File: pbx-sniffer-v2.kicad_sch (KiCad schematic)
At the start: 0 parts

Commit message: finish initial supporting components for mcu
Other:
- sheet MCU ports: added linectrl0, linectrl1, linectrl10, linectrl11, linectrl12, linectrl13, linectrl14, linectrl15, linectrl2, linectrl3, linectrl4, linectrl5, linectrl6, linectrl7, linectrl8, linectrl9, shiftClk, shiftInh, shiftLd, shiftOut, spi0clk, spi0cs0, spi0miso, spi0mosi, usb5V; removed none

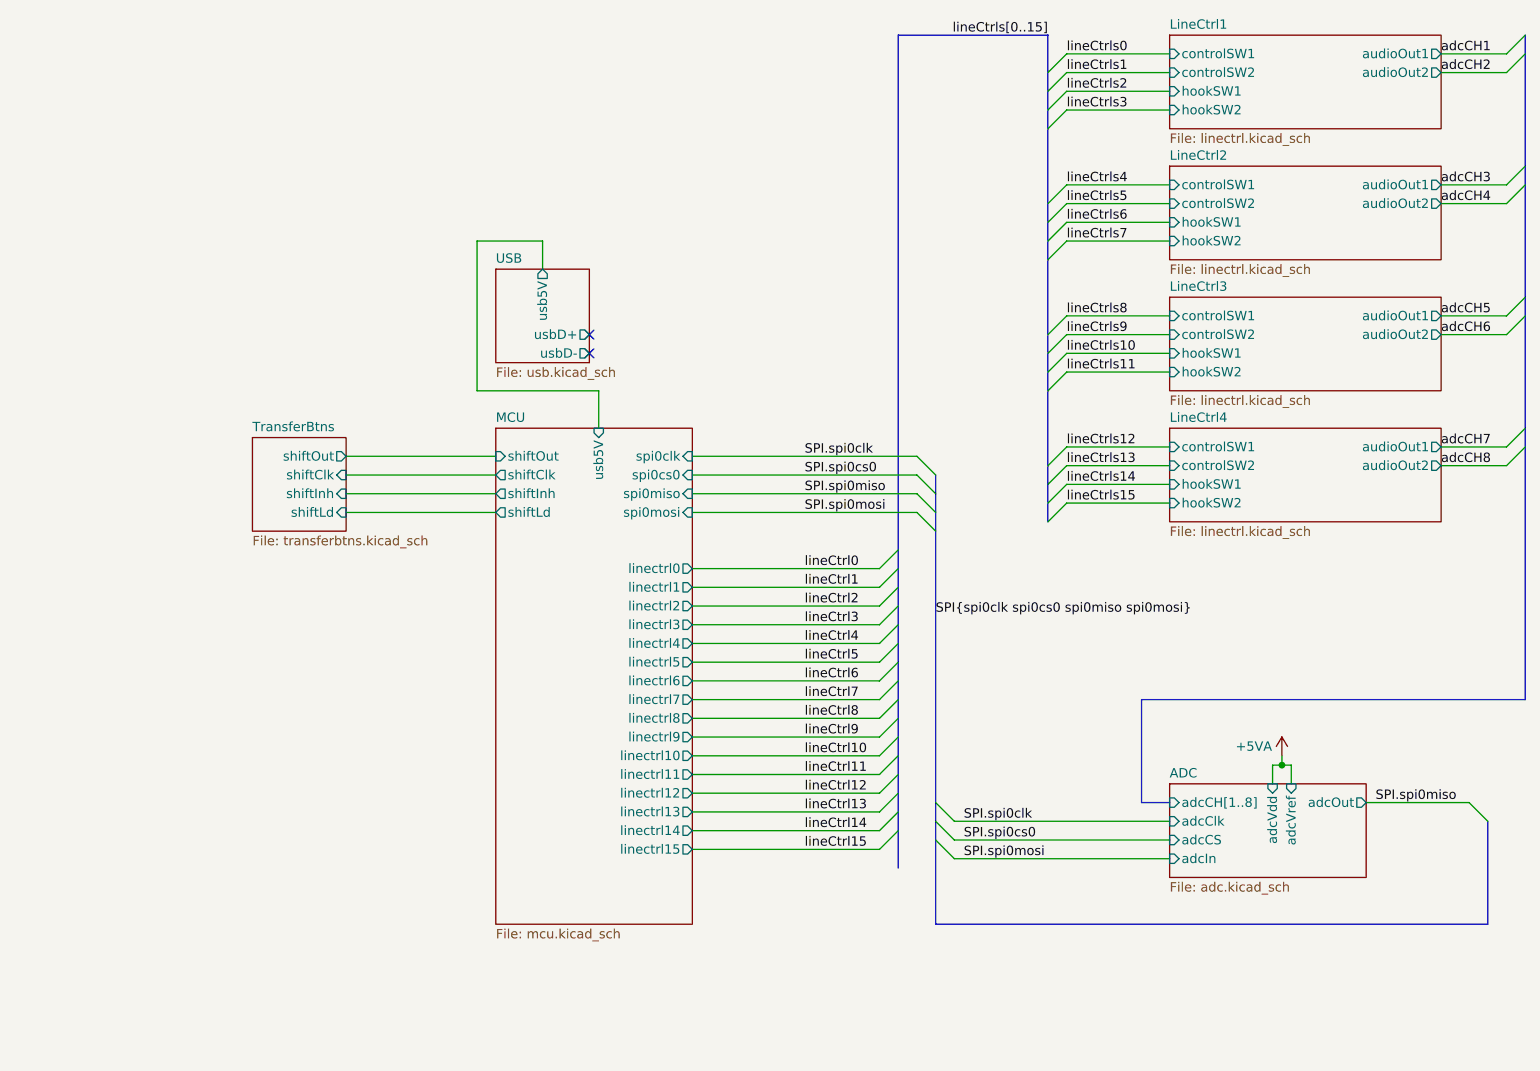
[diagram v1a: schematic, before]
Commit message: fix nearly all erc errors
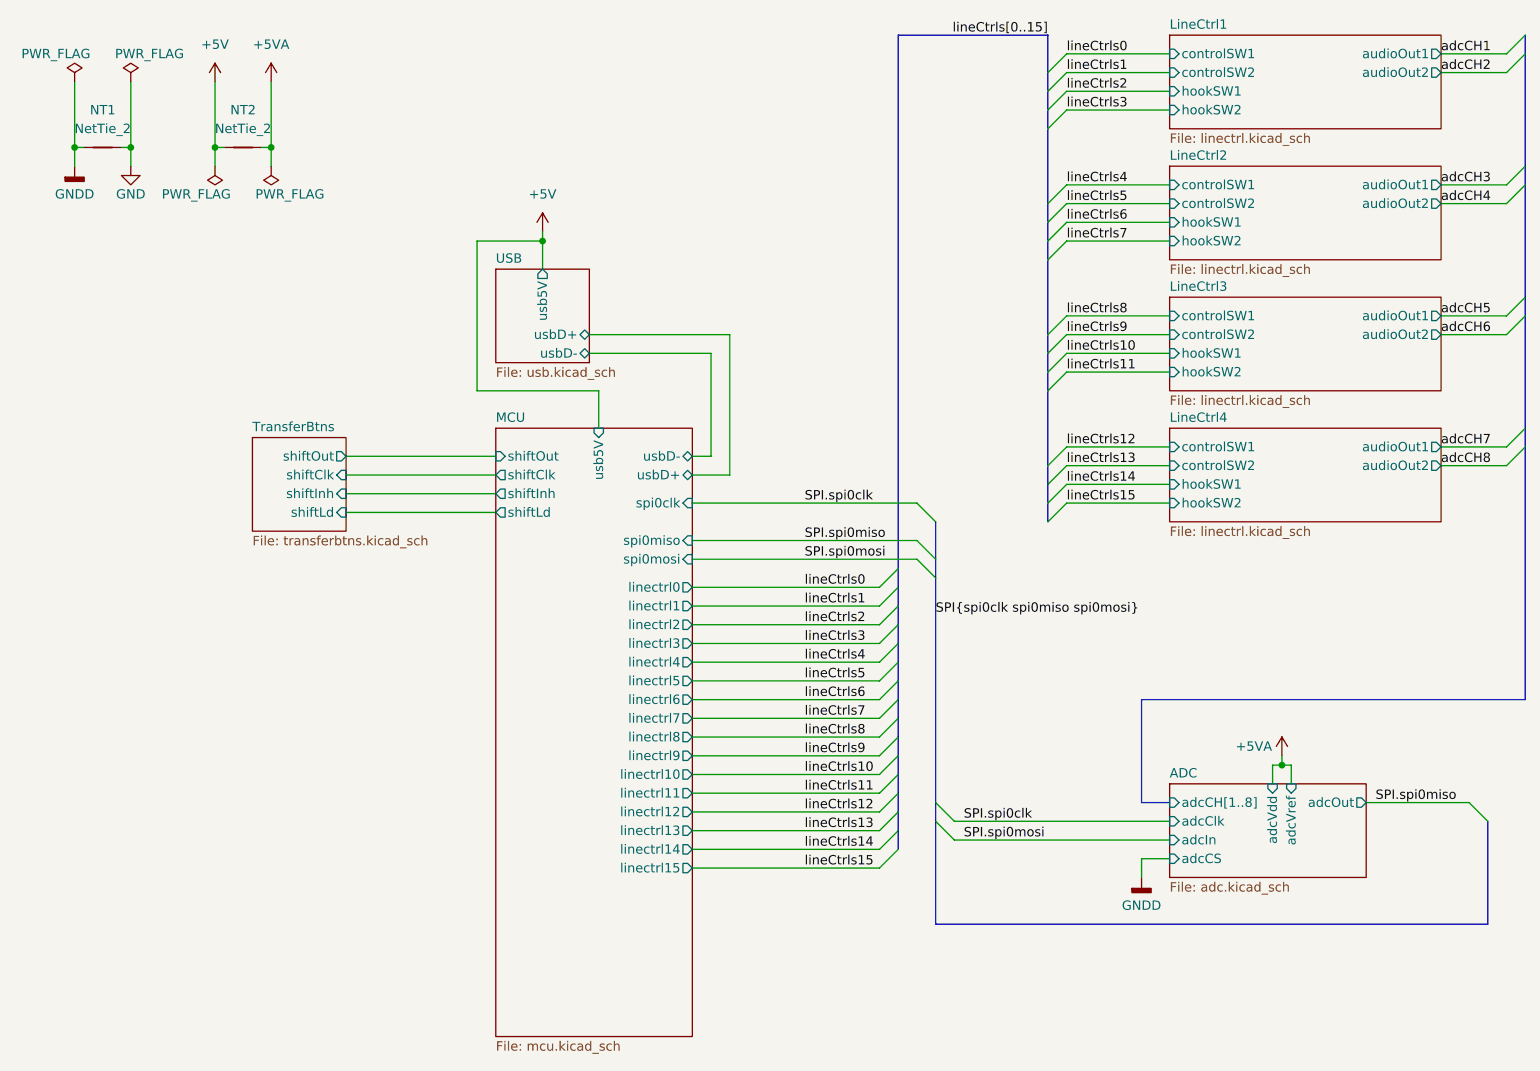
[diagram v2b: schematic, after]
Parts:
- added NT1, NT2: NetTie_2, symbol Device:NetTie_2
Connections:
- net +5VA: now also NT2.2
- new net +5V: NT2.1
- new net GND: NT1.2
- new net GNDD: NT1.1
- no-connect marks 2 -> 0
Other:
- sheet MCU ports: added usbD+, usbD-; removed spi0cs0

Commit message: unsplit grounds, finish power circuitry, start picking footprints/partnumbers
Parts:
- removed NT1, NT2: NetTie_2, symbol Device:NetTie_2
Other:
- added sheet Power (power.kicad_sch)
- sheet MCU ports: added none; removed usb5V

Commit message: added power mux, finished up schematic and picking footprints/partnumbers
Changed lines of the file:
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@@
 		(in_pos_files yes)
 		(dnp no)
-		(property "Reference" "#PWR141"
+		(property "Reference" "#PWR01"
 			(at 175.26 149.86 0)
 			(hide yes)
@@
 			(project "pbx-sniffer-v2"
 				(path "/eb421281-26a1-483f-b39a-0425ec8eb8df"
-					(reference "#PWR141")
+					(reference "#PWR01")
 					(unit 1)
 				)
@@
 		(in_pos_files yes)
 		(dnp no)
-		(property "Reference" "#PWR011"
+		(property "Reference" "#PWR02"
 			(at 194.31 130.81 0)
 			(hide yes)
@@
 			(project "pbx-sniffer-v2"
 				(path "/eb421281-26a1-483f-b39a-0425ec8eb8df"
-					(reference "#PWR011")
+					(reference "#PWR02")
 					(unit 1)
 				)
@@
 			)
 		)
-		(pin "spi0clk" input
+		(pin "spi0clk" output
 			(at 114.3 92.71 0)
 			(effects
@@
 			)
 		)
-		(pin "spi0mosi" input
+		(pin "spi0mosi" output
 			(at 114.3 100.33 0)
 			(effects

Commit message: nearly complete layout lol
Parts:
- added H1, H2, H3, H4: MountingHole, MountingHole:MountingHole_5.3mm_M5_Pad, symbol Mechanical:MountingHole
